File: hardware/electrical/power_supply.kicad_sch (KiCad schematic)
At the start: 31 parts, among them J4 JST-XH, Q1 IRLZ34N, Q2 IRLZ34N, Q3 IRLML5203, Q4 IRLML5203, Q5 2N7002, Q6 AO3401A, U4 MCP73831-2-OT, U5 AP9101CK6, U6 APX803S-31SA-7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

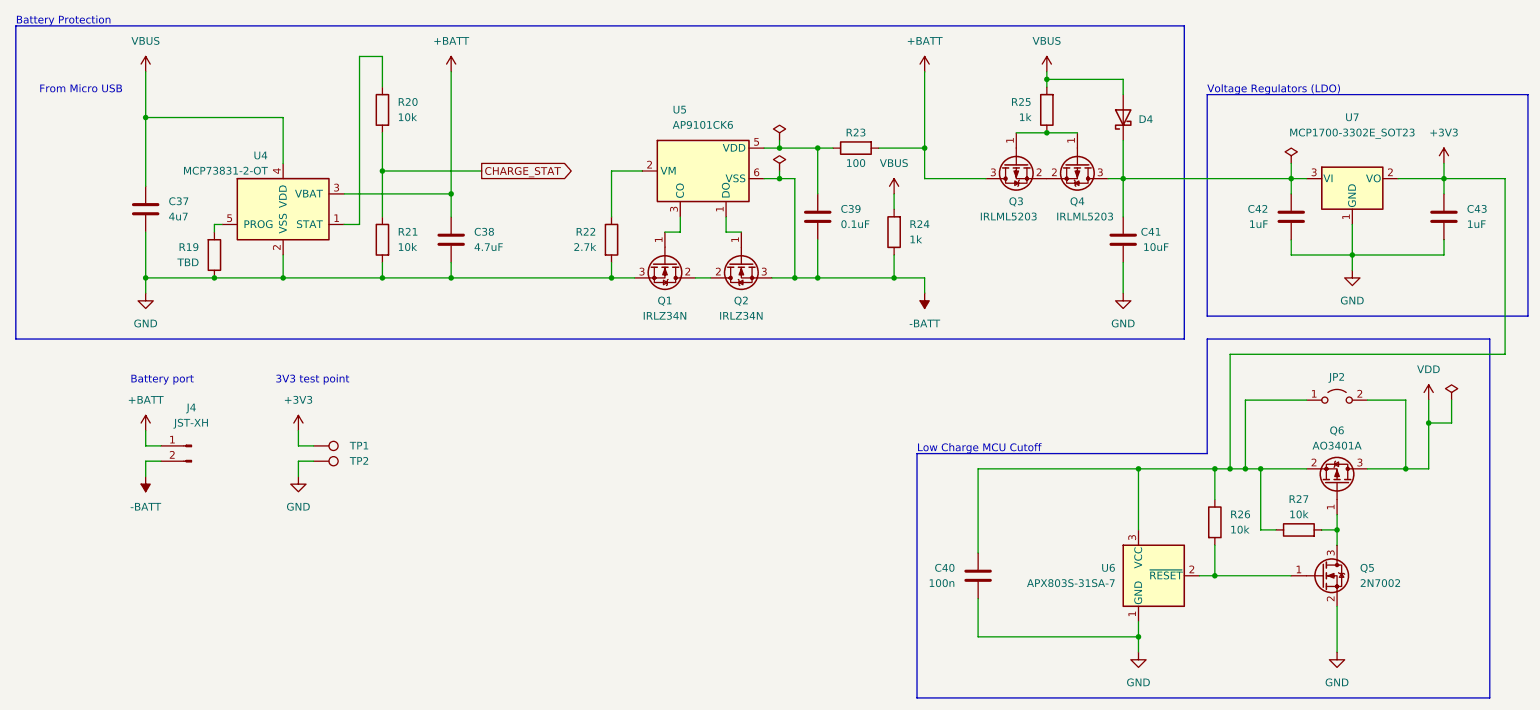
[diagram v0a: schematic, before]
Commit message: Update footprints to KiCad 7.0 versions
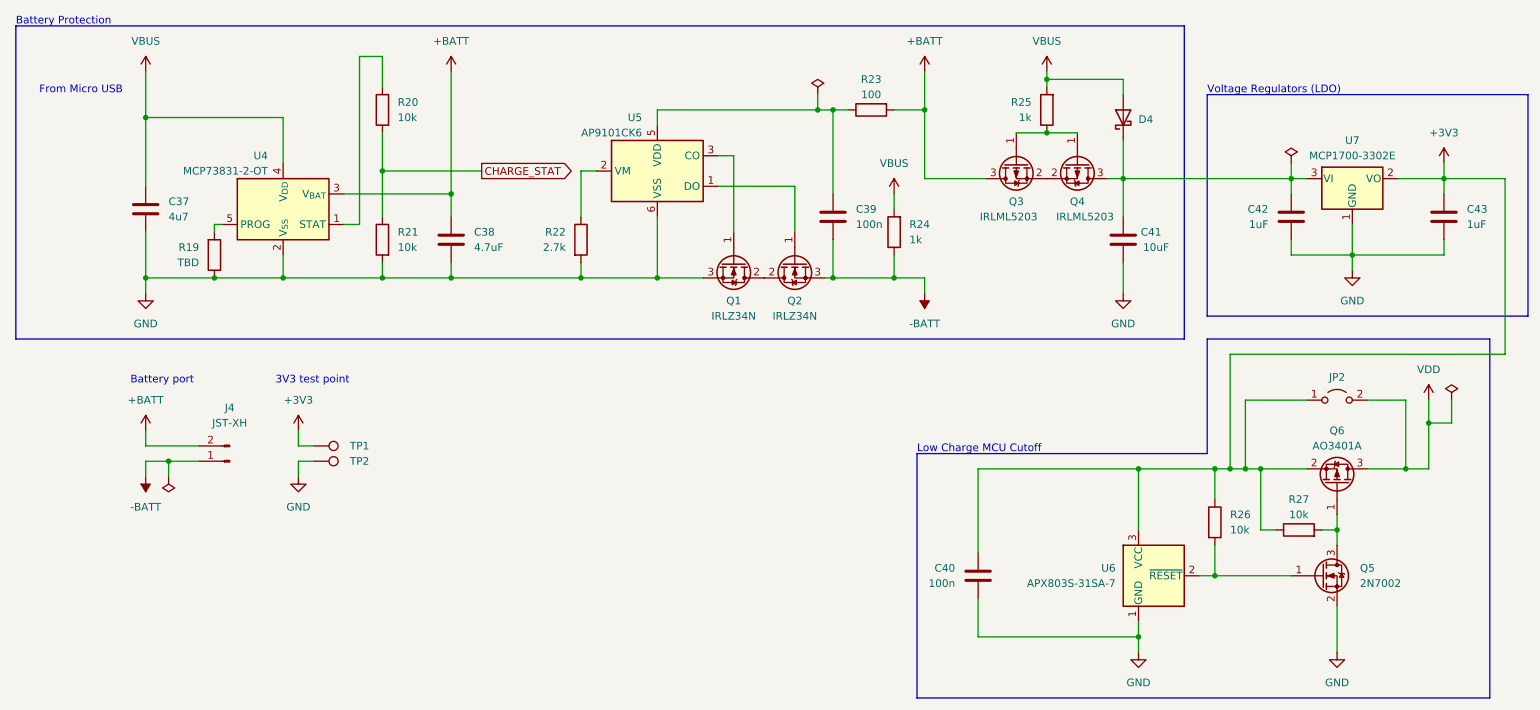
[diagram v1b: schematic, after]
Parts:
- removed J4: JST-XH, Connector_PinHeader_2.00mm:PinHeader_1x02_P2.00mm_Vertical, symbol Connector:Conn_01x02_Male
- removed U7: MCP1700-3302E_SOT23, Package_TO_SOT_SMD:SOT-23, symbol Regulator_Linear:MCP1700-3302E_SOT23
- added J4: JST-XH, symbol Connector:Conn_01x02_Pin
- added U7: MCP1700-3302E, Package_TO_SOT_SMD:SOT-23, symbol Regulator_Linear:MCP1700x-330xxTT
- C39: value 0.1uF -> 100n
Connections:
- net +3V3: now also U7.2 (VO)
- net +BATT: now also J4.2 (Pin_2)
- net -BATT: now also J4.1 (Pin_1); no longer U5.6 (VSS)
- net GND: now also U5.6 (VSS), U7.1 (GND)
- net at C41.2, C42.2, D4.1 (K)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: now also U7.3 (VI)
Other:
- moved on the sheet: C39, Q1, Q2, R22, R23, U5

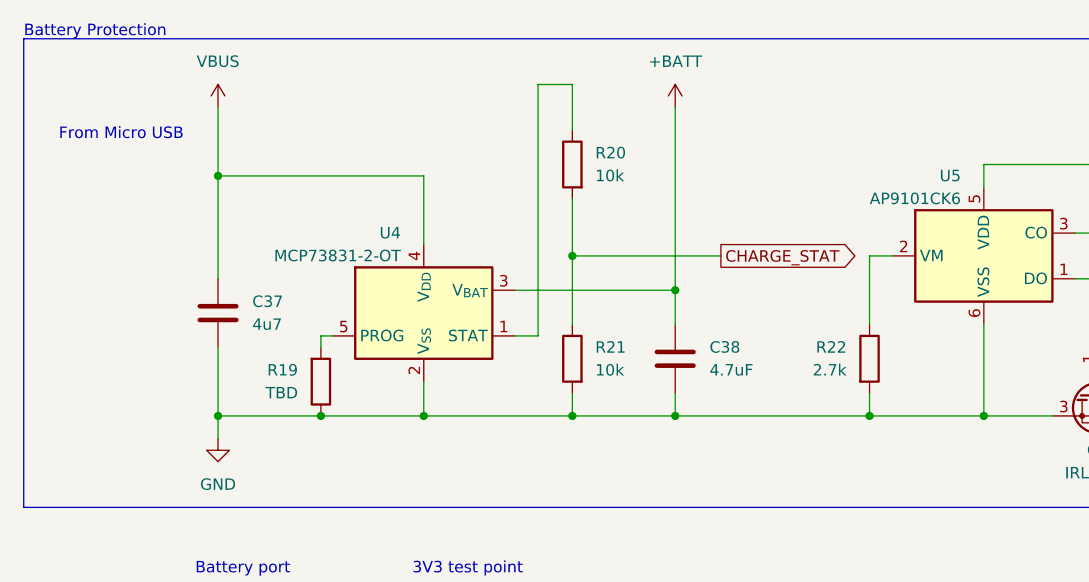
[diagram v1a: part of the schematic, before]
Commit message: updated charger IC
note on charge status signal:
LOW when charging
HIGH when charge cycle completed or USB not connected
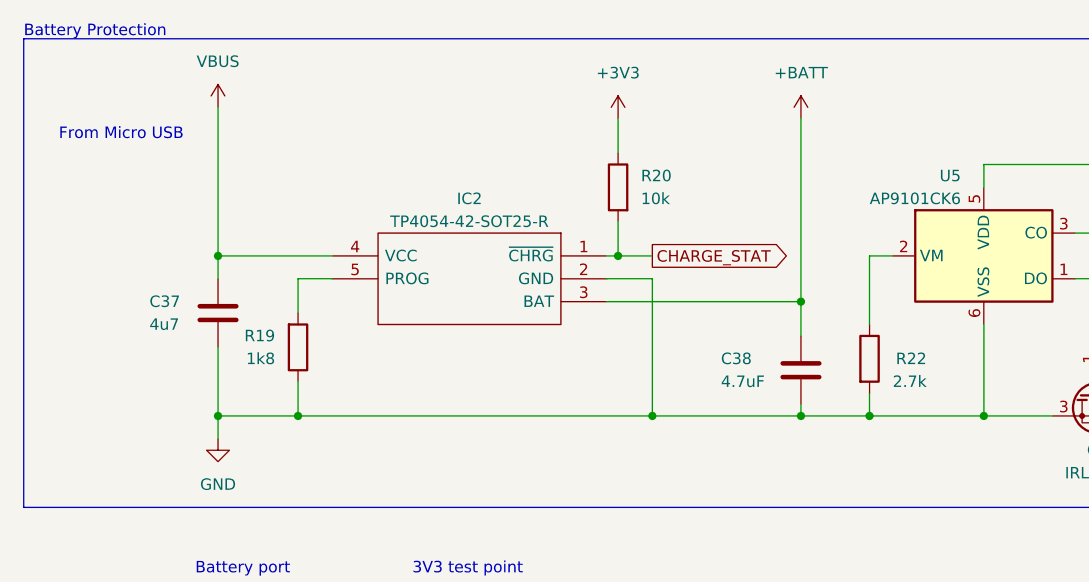
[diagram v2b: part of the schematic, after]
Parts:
- removed R21: 10k, Resistor_SMD:R_0805_2012Metric_Pad1.20x1.40mm_HandSolder, symbol Device:R
- removed U4: MCP73831-2-OT, Package_TO_SOT_SMD:SOT-23-5, symbol Battery_Management:MCP73831-2-OT
- added IC2: TP4054-42-SOT25-R, SamacSys_Parts:SOT95P280X100-5N, symbol SamacSys_Parts:TP4054-42-SOT25-R
- R19: value TBD -> 1k8
- R20: footprint Resistor_SMD:R_0805_2012Metric_Pad1.20x1.40mm_HandSolder -> Resistor_SMD:R_0402_1005Metric; LCSC Part # (none) -> C25744; Mfr (none) -> UNI-ROYAL(Uniroyal Elec); Mfr. Part # (none) -> 0402WGF1002TCE
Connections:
- net +3V3: now also R20.1
- net +BATT: now also IC2.3 (BAT)
- net CHARGE_STAT: now also IC2.1 (~{CHRG})
- net GND: now also IC2.2 (GND)
- net VBUS: now also IC2.4 (VCC)
- net at R19.2: now also IC2.5 (PROG)
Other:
- moved on the sheet: C38, R19

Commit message: Replace TP4054 symbol with custom symbol
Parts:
- removed IC2: TP4054-42-SOT25-R, SamacSys_Parts:SOT95P280X100-5N, symbol SamacSys_Parts:TP4054-42-SOT25-R
- added U2: TP4054, Package_TO_SOT_SMD:SOT-23-5, symbol 3885:TP4054-42-SOT25R
- R23: value 100 -> 100R
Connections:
- net +BATT: now also U2.3 (BAT)
- net CHARGE_STAT: now also U2.1 (~{CHRG})
- net GND: now also U2.2 (GND)
- net VBUS: now also U2.4 (VCC)
- net at R19.2: now also U2.5 (PROG)
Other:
- moved on the sheet: C38, C39, R19, R20

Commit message: Replace 3.3V regulator with AMS1117-3.3 and use more readily available capacitor values
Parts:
- removed C41: 10uF, Capacitor_SMD:C_0402_1005Metric, symbol Device:C
- removed U7: MCP1700-3302E, Package_TO_SOT_SMD:SOT-23, symbol Regulator_Linear:MCP1700x-330xxTT
- added U7: AMS1117-3.3, Package_TO_SOT_SMD:SOT-223-3_TabPin2, symbol Regulator_Linear:AMS1117-3.3
- C37: value 4u7 -> 10u
- C38: value 4.7uF -> 10u
- C42, C43: value 1uF -> 10u
- R22: value 2.7k -> 2k7
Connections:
- net +3V3: now also U7.2 (VO)
- net GND: now also U7.1 (GND)
- net at C42.2, D4.1 (K), Q4.3 (D): now also U7.3 (VI)

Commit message: Revert "Replace 3.3V regulator with AMS1117-3.3 and use more readily available capacitor values"
This reverts commit 29fecb9214ea02ba74fbe5bb5a2b4ebe43046313.
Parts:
- removed U7: AMS1117-3.3, Package_TO_SOT_SMD:SOT-223-3_TabPin2, symbol Regulator_Linear:AMS1117-3.3
- added C41: 10uF, Capacitor_SMD:C_0402_1005Metric, symbol Device:C
- added U7: MCP1700-3302E, Package_TO_SOT_SMD:SOT-23, symbol Regulator_Linear:MCP1700x-330xxTT
- C37: value 10u -> 4u7
- C38: value 10u -> 4.7uF
- C42, C43: value 10u -> 1uF
- R22: value 2k7 -> 2.7k
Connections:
- net +3V3: now also U7.2 (VO)
- net GND: now also C41.1, U7.1 (GND)
- net at C42.2, D4.1 (K), Q4.3 (D): now also C41.2, U7.3 (VI)
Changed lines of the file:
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@@
-    (stroke (width 0) (type default))
-  )
-  (wire (pts (xy 229.87 50.8) (xy 229.87 53.34))
     (stroke (width 0) (type default))
   )
@@
     (stroke (width 0) (type default))
   )
+  (wire (pts (xy 229.87 50.8) (xy 232.41 50.8))
+    (stroke (width 0) (type default))
+  )
   (wire (pts (xy 74.93 34.29) (xy 74.93 38.1))
     (stroke (width 0) (type default))
@@
     (stroke (width 0) (type default))
   )
+  (wire (pts (xy 201.93 69.85) (xy 201.93 64.77))
+    (stroke (width 0) (type default))
+  )
   (wire (pts (xy 168.91 67.31) (xy 168.91 69.85))
     (stroke (width 0) (type default))
@@
     (stroke (width 0) (type default))
   )
-  (wire (pts (xy 229.87 50.8) (xy 232.41 50.8))
-    (stroke (width 0) (type default))
-  )
   (wire (pts (xy 242.57 99.06) (xy 248.92 99.06))
     (stroke (width 0) (type default))
@@
     (stroke (width 0) (type default))
   )
+  (wire (pts (xy 229.87 53.34) (xy 229.87 50.8))
+    (stroke (width 0) (type default))
+  )
   (wire (pts (xy 39.37 49.53) (xy 52.07 49.53))
+    (stroke (width 0) (type default))
+  )
+  (wire (pts (xy 201.93 57.15) (xy 201.93 50.8))
     (stroke (width 0) (type default))
   )
@@
     )
   )
+  (symbol (lib_id "power:GND") (at 201.93 69.85 0) (mirror y) (unit 1)
+    (in_bom yes) (on_board yes) (dnp no) (fields_autoplaced)
+    (property "Reference" "#PWR077" (at 201.93 76.2 0)
+      (effects (font (size 1.27 1.27)) hide)
+    )
+    (property "Value" "GND" (at 201.93 74.93 0)
+      (effects (font (size 1.27 1.27)))
+    )
+    (property "Footprint" "" (at 201.93 69.85 0)
+      (effects (font (size 1.27 1.27)) hide)
+    )
+    (property "Datasheet" "" (at 201.93 69.85 0)
+      (effects (font (size 1.27 1.27)) hide)
+    )
+    (pin "1")
+    (instances
+      (project "3885"
+        (path "/7363a4f0-2da1-4086-abed-ea6709c3a185/0217b7ef-3928-43d6-9a5a-467bfde0e5ea"
+          (reference "#PWR077") (unit 1)
+        )
+      )
+    )
+  )
   (symbol (lib_id "Device:C") (at 229.87 57.15 0) (mirror x) (unit 1)
     (in_bom yes) (on_board yes) (dnp no)
@@
       (effects (font (size 1.27 1.27)) (justify right))
     )
-    (property "Value" "10u" (at 226.06 58.42 0)
+    (property "Value" "1uF" (at 226.06 58.42 0)
       (effects (font (size 1.27 1.27)) (justify right))
     )
@@
       (effects (font (size 1.27 1.27)) (justify left))
     )
-    (property "Value" "2k7" (at 114.3 62.23 0)
+    (property "Value" "2.7k" (at 114.3 62.23 0)
       (effects (font (size 1.27 1.27)) (justify left))
     )
@@
       (effects (font (size 1.27 1.27)) (justify right))
     )
-    (property "Value" "10u" (at 91.44 63.5 0)
+    (property "Value" "4.7uF" (at 91.44 63.5 0)
       (effects (font (size 1.27 1.27)) (justify right))
     )
@@
       (effects (font (size 1.27 1.27)) (justify left))
     )
-    (property "Value" "10u" (at 259.08 58.42 0)
+    (property "Value" "1uF" (at 259.08 58.42 0)
       (effects (font (size 1.27 1.27)) (justify left))
     )
@@
         (path "/7363a4f0-2da1-4086-abed-ea6709c3a185/0217b7ef-3928-43d6-9a5a-467bfde0e5ea"
           (reference "C43") (unit 1)
+        )
+      )
+    )
+  )
+  (symbol (lib_id "Regulator_Linear:MCP1700x-330xxTT") (at 240.03 50.8 0) (unit 1)
+    (in_bom yes) (on_board yes) (dnp no) (fields_autoplaced)
+    (property "Reference" "U7" (at 240.03 44.45 0)
+      (effects (font (size 1.27 1.27)))
+    )
+    (property "Value" "MCP1700-3302E" (at 240.03 46.99 0)
+      (effects (font (size 1.27 1.27)))
+    )
+    (property "Footprint" "Package_TO_SOT_SMD:SOT-23" (at 240.03 45.085 0)
+      (effects (font (size 1.27 1.27)) hide)
+    )
+    (property "Datasheet" "http://ww1.microchip.com/downloads/en/DeviceDoc/20001826D.pdf" (at 240.03 50.8 0)
+      (effects (font (size 1.27 1.27)) hide)
+    )
+    (pin "1")
+    (pin "2")
+    (pin "3")
+    (instances
+      (project "3885"
+        (path "/7363a4f0-2da1-4086-abed-ea6709c3a185/0217b7ef-3928-43d6-9a5a-467bfde0e5ea"
+          (reference "U7") (unit 1)
+        )
+      )
+    )
+  )
+  (symbol (lib_id "Device:C") (at 201.93 60.96 0) (mirror x) (unit 1)
+    (in_bom yes) (on_board yes) (dnp no)
+    (property "Reference" "C41" (at 208.28 59.69 0)
+      (effects (font (size 1.27 1.27)) (justify right))
+    )
+    (property "Value" "10uF" (at 209.55 62.23 0)
+      (effects (font (size 1.27 1.27)) (justify right))
+    )
+    (property "Footprint" "Capacitor_SMD:C_0402_1005Metric" (at 202.8952 57.15 0)
+      (effects (font (size 1.27 1.27)) hide)
+    )
+    (property "Datasheet" "~" (at 201.93 60.96 0)
+      (effects (font (size 1.27 1.27)) hide)
+    )
+    (pin "1")
+    (pin "2")
+    (instances
+      (project "3885"
+        (path "/7363a4f0-2da1-4086-abed-ea6709c3a185/0217b7ef-3928-43d6-9a5a-467bfde0e5ea"
+          (reference "C41") (unit 1)
         )
       )
@@
       (effects (font (size 1.27 1.27)) (justify left))
     )
-    (property "Value" "10u" (at 31.75 57.15 0)
+    (property "Value" "4u7" (at 31.75 57.15 0)
       (effects (font (size 1.27 1.27)) (justify left))
     )
@@
         )
       )
-    )
-  )
-  (symbol (lib_id "Regulator_Linear:AMS1117-3.3") (at 240.03 50.8 0) (unit 1)
-    (in_bom yes) (on_board yes) (dnp no) (fields_autoplaced)
-    (property "Reference" "U7" (at 240.03 44.45 0)
-      (effects (font (size 1.27 1.27)))
-    )
-    (property "Value" "AMS1117-3.3" (at 240.03 46.99 0)
-      (effects (font (size 1.27 1.27)))
-    )
-    (property "Footprint" "Package_TO_SOT_SMD:SOT-223-3_TabPin2" (at 240.03 45.72 0)
-      (effects (font (size 1.27 1.27)) hide)
-    )
-    (property "Datasheet" "http://www.advanced-monolithic.com/pdf/ds1117.pdf" (at 242.57 57.15 0)
-      (effects (font (size 1.27 1.27)) hide)
-    )
-    (pin "1")
-    (pin "2")
-    (pin "3")
-    (instances
-      (project "3885"
-        (path "/7363a4f0-2da1-4086-abed-ea6709c3a185/0217b7ef-3928-43d6-9a5a-467bfde0e5ea"
-          (reference "U7") (unit 1)
-        )
-      )

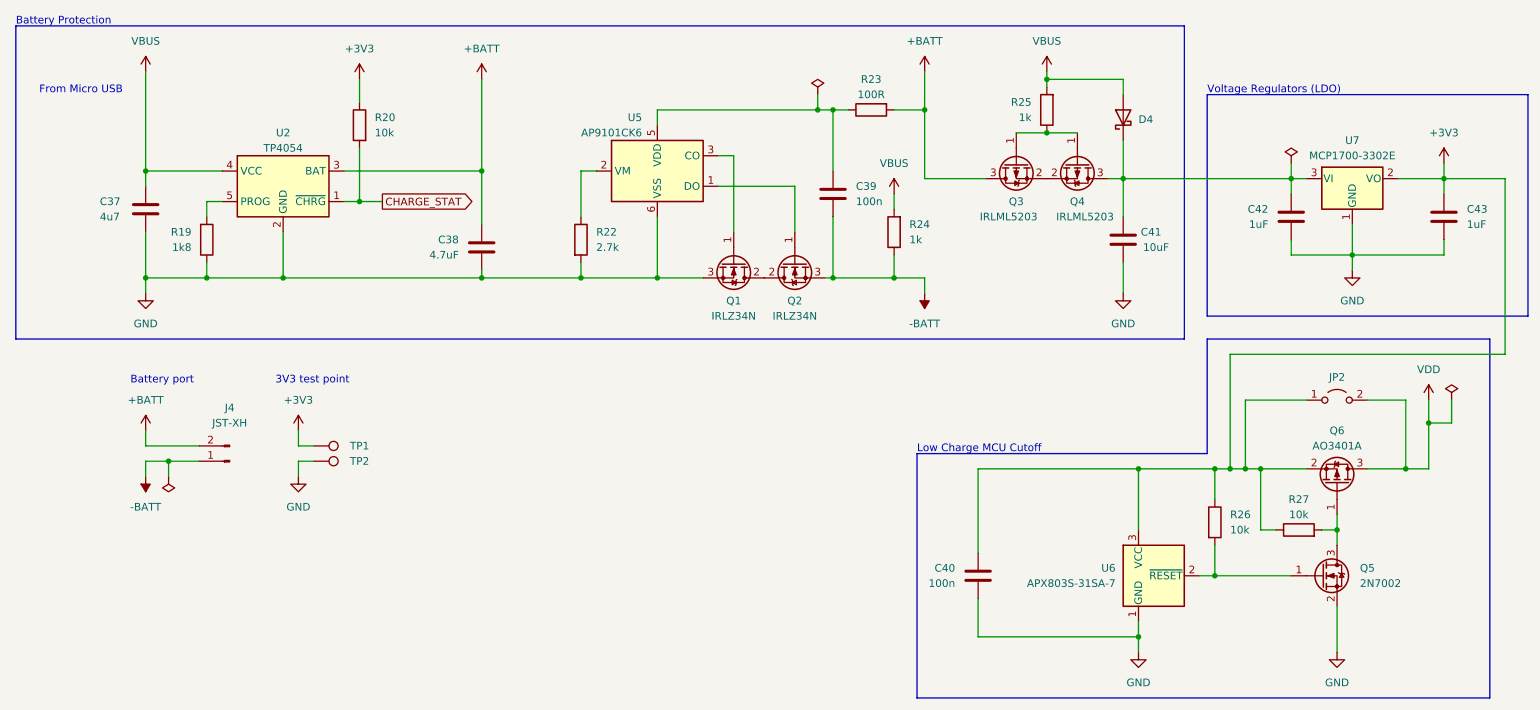
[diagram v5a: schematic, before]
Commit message: Replace 3.3V regulator with WL2803E
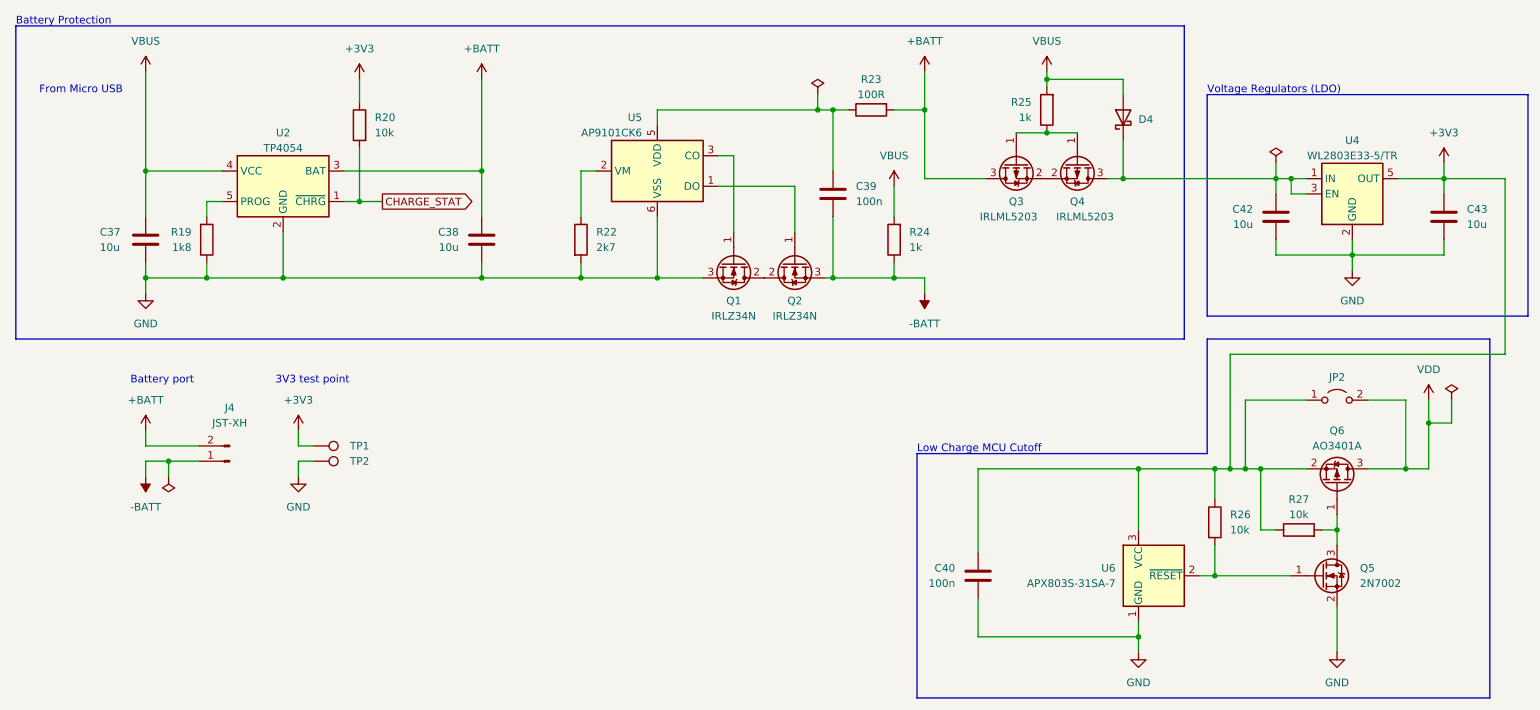
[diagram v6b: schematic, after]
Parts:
- removed C41: 10uF, Capacitor_SMD:C_0402_1005Metric, symbol Device:C
- removed U7: MCP1700-3302E, Package_TO_SOT_SMD:SOT-23, symbol Regulator_Linear:MCP1700x-330xxTT
- added U4: WL2803E33-5/TR, Package_TO_SOT_SMD:SOT-23-5, symbol 3885:WL2803E
- C37: value 4u7 -> 10u
- C38: value 4.7uF -> 10u
- C42, C43: value 1uF -> 10u
- R22: value 2.7k -> 2k7
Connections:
- net +3V3: now also U4.5 (OUT)
- net GND: now also U4.2 (GND)
- net at C42.2, D4.1 (K), Q4.3 (D): now also U4.1 (IN), U4.3 (EN)
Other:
- moved on the sheet: C37, C38, C42, R24
